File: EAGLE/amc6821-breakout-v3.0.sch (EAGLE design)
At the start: 38 parts, among them J8 QWIIC_RIGHT_ANGLE, J9 QWIIC_RIGHT_ANGLE, Q1 2N3904, U1 AMC6821-Q1QSOP-16N, U3 AP2112K-3.3

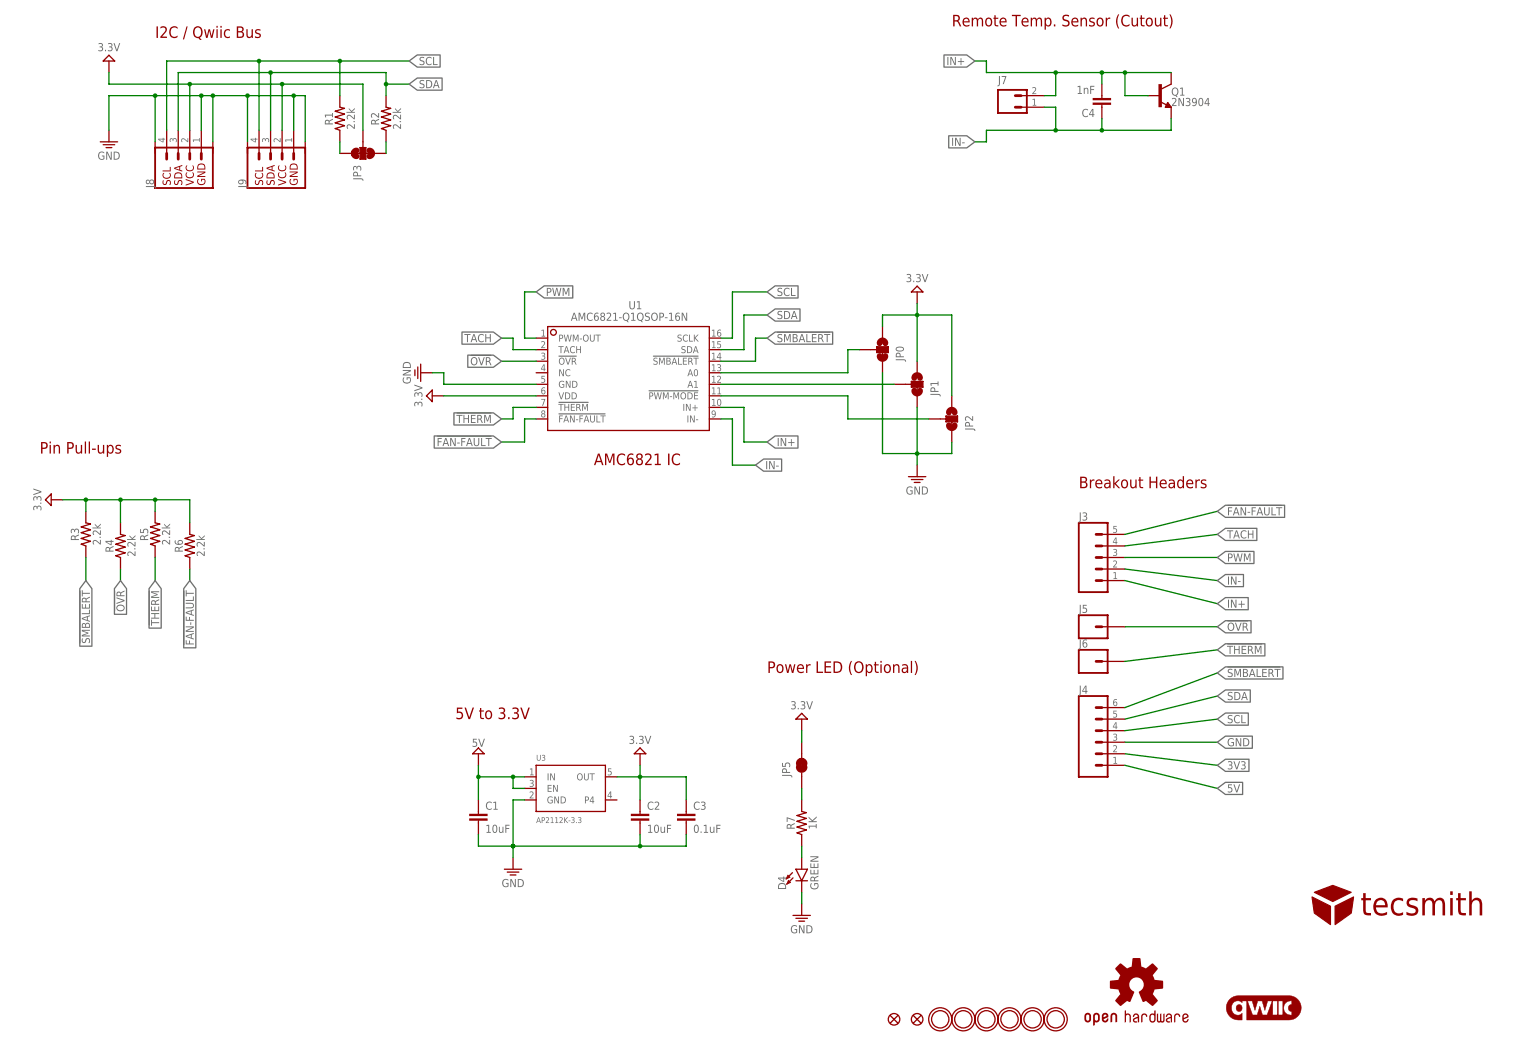
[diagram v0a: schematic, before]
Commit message: move C3 closer to the IC
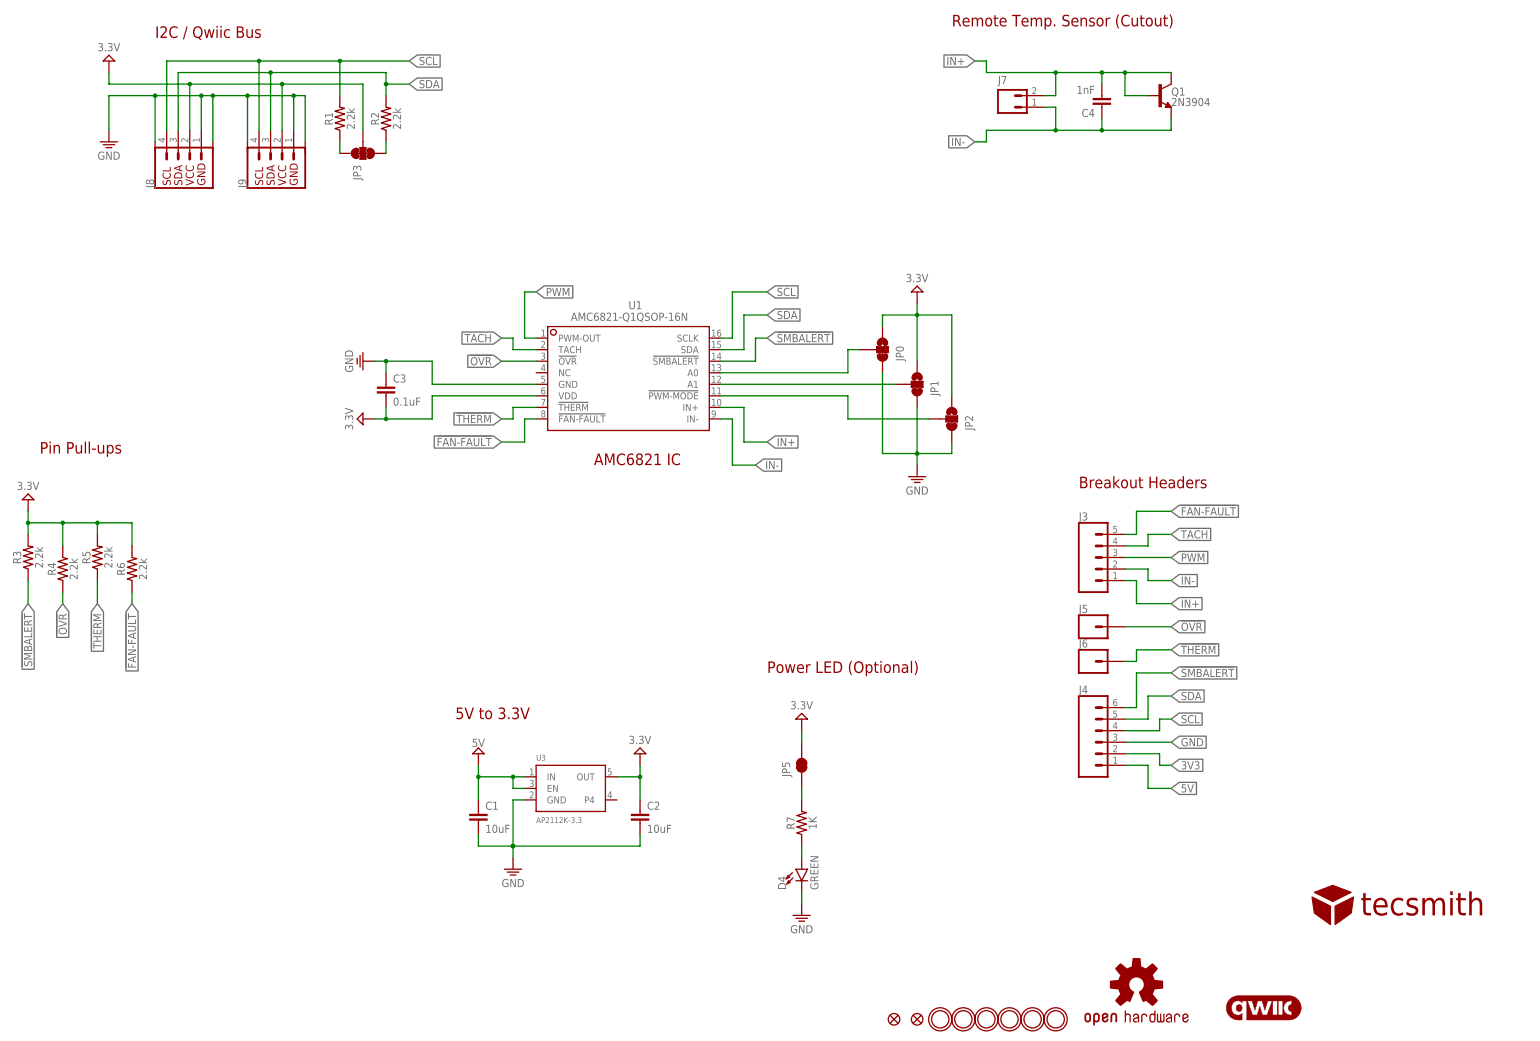
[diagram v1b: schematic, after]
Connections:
- net 3V3: now also C3.2; no longer C3.1
- net GND: now also C3.1; no longer C3.2
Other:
- moved on the sheet: C3, R3, R4, R5, R6

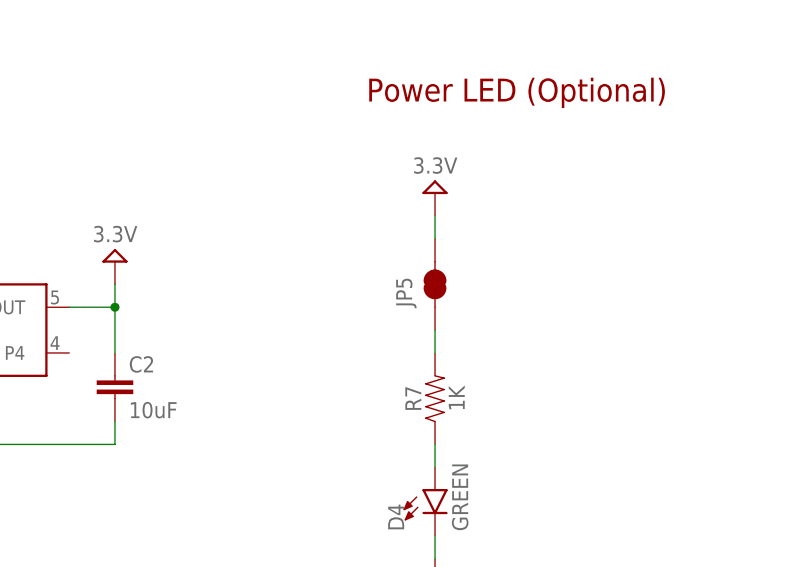
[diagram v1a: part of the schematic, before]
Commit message: minor rename, JP4
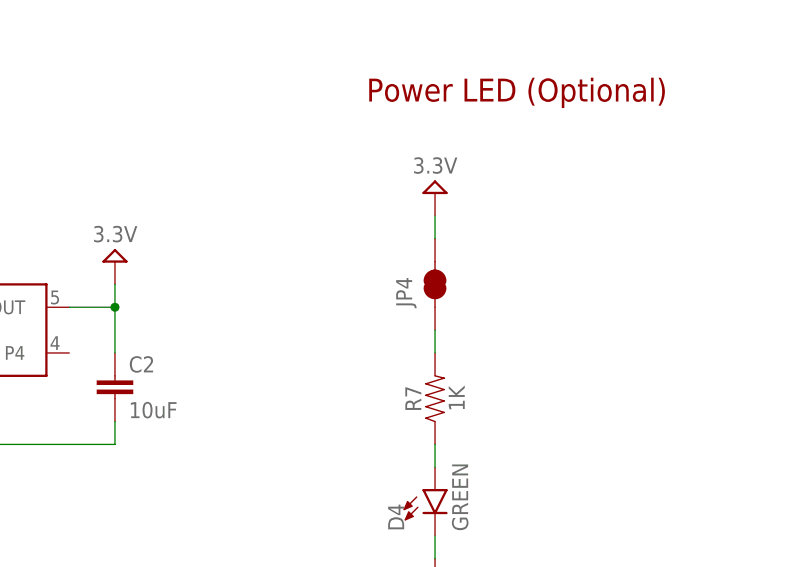
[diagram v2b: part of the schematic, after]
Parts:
- renumbered JP5 to JP4
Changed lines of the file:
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@@
 <part name="D4" library="SparkFun-LED" deviceset="LED-GREEN" device="0603" value="GREEN"/>
 <part name="R7" library="SparkFun-Resistors" deviceset="RESISTOR" device="0805" value="1K"/>
-<part name="JP5" library="SparkFun-Jumpers" deviceset="JUMPER-SMT_2_NC_TRACE" device="_SILK" package3d_urn="urn:adsk.eagle:package:39281/1"/>
+<part name="JP4" library="SparkFun-Jumpers" deviceset="JUMPER-SMT_2_NC_TRACE" device="_SILK" package3d_urn="urn:adsk.eagle:package:39281/1"/>
 <part name="FRAME1" library="frames" library_urn="urn:adsk.eagle:library:229" deviceset="A3L-LOC" device=""/>
 <part name="U$1" library="VinoRodrigues_Custom_Eagle" deviceset="TECSMITH-LOGO" device=""/>
@@
 <attribute name="VALUE" x="230.124" y="50.8" size="1.778" layer="96" font="vector" rot="R90" align="top-center"/>
 </instance>
-<instance part="JP5" gate="G$1" x="228.6" y="63.5" smashed="yes" rot="R90">
+<instance part="JP4" gate="G$1" x="228.6" y="63.5" smashed="yes" rot="R90">
 <attribute name="NAME" x="226.06" y="60.96" size="1.778" layer="95" font="vector" rot="R90"/>
 </instance>
@@
 <segment>
 <pinref part="SUPPLY5" gate="G$1" pin="VCC"/>
-<pinref part="JP5" gate="G$1" pin="2"/>
+<pinref part="JP4" gate="G$1" pin="2"/>
 <wire x1="228.6" y1="71.12" x2="228.6" y2="68.58" width="0.1524" layer="91"/>
 </segment>
@@
 <net name="N$12" class="0">
 <segment>
-<pinref part="JP5" gate="G$1" pin="1"/>
+<pinref part="JP4" gate="G$1" pin="1"/>
 <pinref part="R7" gate="G$1" pin="2"/>
 <wire x1="228.6" y1="55.88" x2="228.6" y2="58.42" width="0.1524" layer="91"/>

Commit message: updates
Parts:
- removed FID3, FID4: FIDUCIAL_1MM, microbuilder:FIDUCIAL_1MM
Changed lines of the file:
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@@
 <part name="U$4" library="microbuilder" deviceset="MOUNTINGHOLE" device="2.5"/>
 <part name="U$8" library="microbuilder" deviceset="MOUNTINGHOLE" device="2.5"/>
-<part name="FID3" library="microbuilder" deviceset="FIDUCIAL" device="_1MM"/>
-<part name="FID4" library="microbuilder" deviceset="FIDUCIAL" device="_1MM"/>
 <part name="U$9" library="microbuilder" deviceset="MOUNTINGHOLE" device="2.5"/>
 <part name="U$10" library="microbuilder" deviceset="MOUNTINGHOLE" device="2.5"/>
@@
 <instance part="U$4" gate="G$1" x="259.08" y="7.62" smashed="yes"/>
 <instance part="U$8" gate="G$1" x="274.32" y="7.62" smashed="yes"/>
-<instance part="FID3" gate="G$1" x="254" y="7.62" smashed="yes"/>
-<instance part="FID4" gate="G$1" x="248.92" y="7.62" smashed="yes"/>
 <instance part="U$9" gate="G$1" x="279.4" y="7.62" smashed="yes"/>
 <instance part="U$10" gate="G$1" x="284.48" y="7.62" smashed="yes"/>
